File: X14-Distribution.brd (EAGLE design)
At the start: 152.4 x 76.2 mm, 57 parts, among them Q1 310mA/60V/1.6Ω, Q2 IRF1018EPBF, Q3 IRF1018EPBF, Q4 IRF1018EPBF, Q5 IRLML5203, Q6 IRLML5203, Q7 IRLML5203, Q8 IRLML5203, U1 DIST_OR_CONTROL_ALTMK06A-M, U2 DIST_OR_CONTROL_ALTMK06A-M

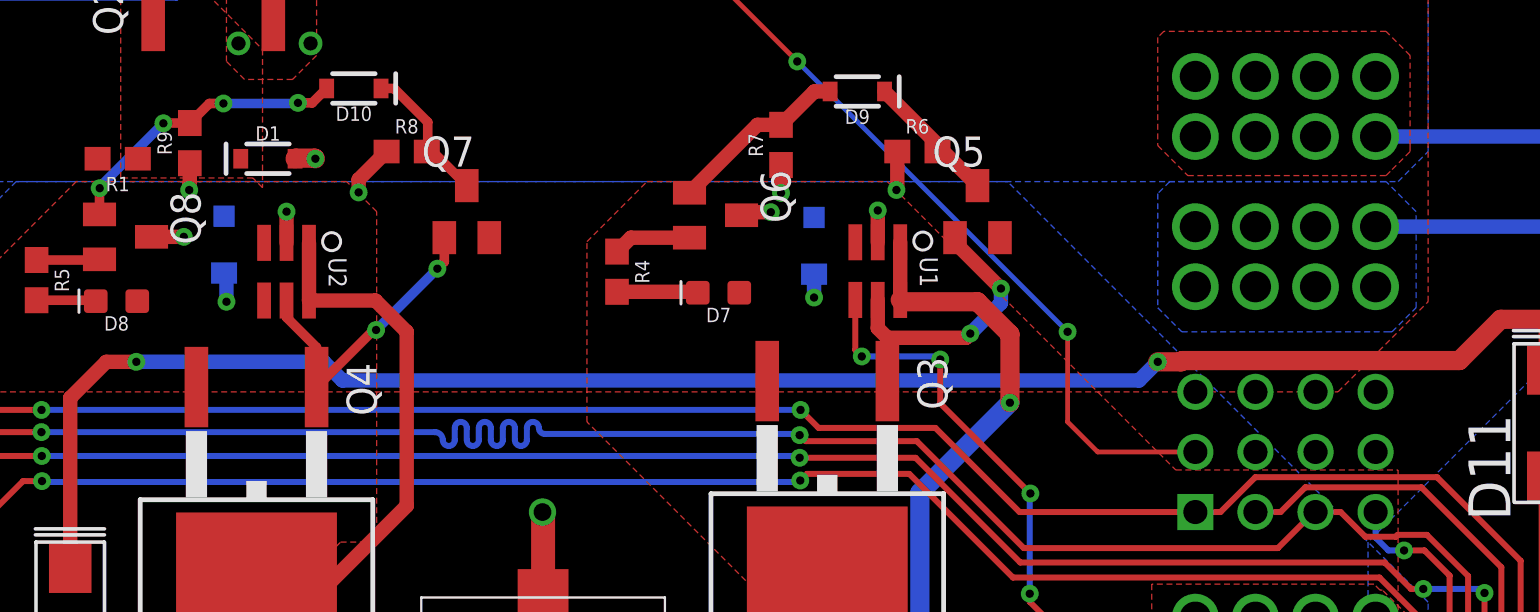
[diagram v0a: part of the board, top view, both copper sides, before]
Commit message: Made changes according to Grant's notes
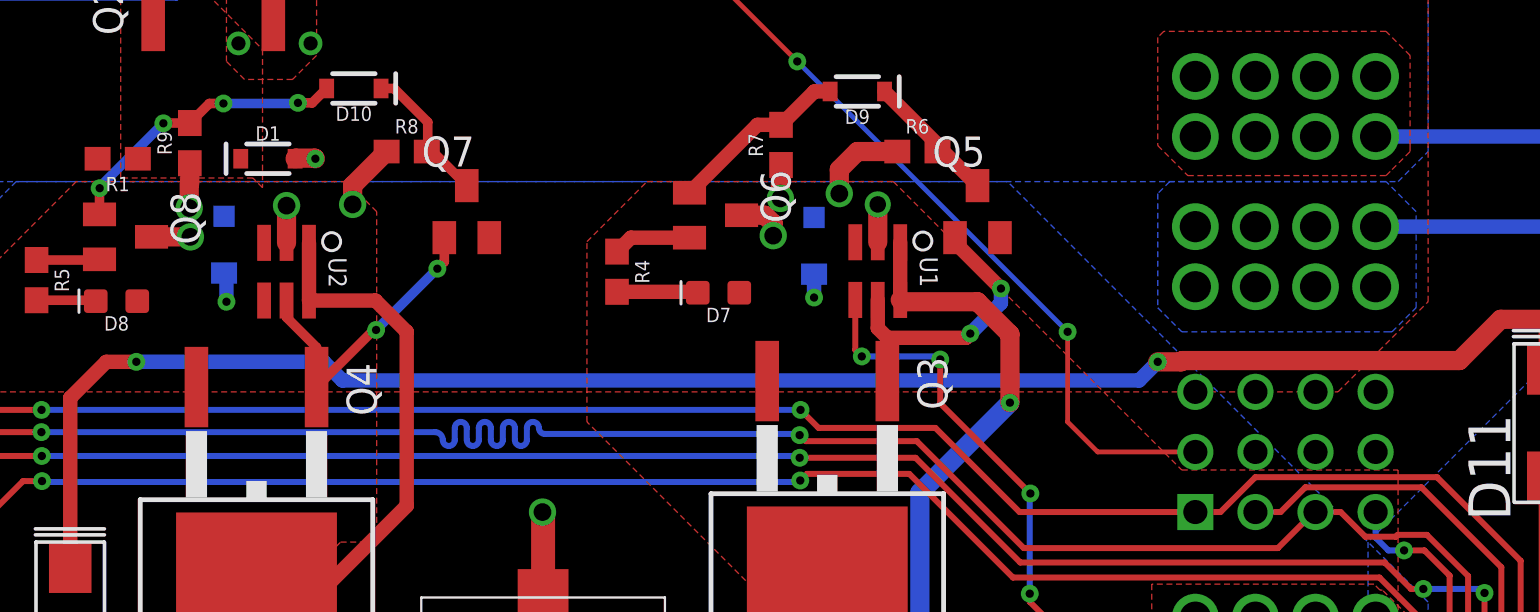
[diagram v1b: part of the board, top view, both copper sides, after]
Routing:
- net 12V_GND: track 63.3 -> 68.5 mm
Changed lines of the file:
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@@
 <wire x1="137.3378" y1="15.0114" x2="138.6586" y2="15.0114" width="0.6096" layer="1"/>
 <wire x1="138.6586" y1="15.0114" x2="140.97" y2="12.7" width="0.6096" layer="1"/>
-<wire x1="65.4128" y1="45.9232" x2="66.7766" y2="45.9232" width="0.6096" layer="1"/>
-<via x="66.7766" y="45.9232" extent="1-16" drill="0.35"/>
-<wire x1="67.0306" y1="49.0356" x2="67.0306" y2="48.1838" width="0.6096" layer="1"/>
+<wire x1="65.4128" y1="45.9232" x2="67.056" y2="45.9232" width="0.8128" layer="1"/>
+<via x="67.056" y="45.9232" extent="1-16" drill="0.75"/>
+<wire x1="67.0306" y1="49.0356" x2="67.0306" y2="48.1838" width="0.8128" layer="1"/>
 <wire x1="67.0306" y1="48.1838" x2="67.0052" y2="48.1584" width="0.6096" layer="1"/>
-<wire x1="67.0052" y1="48.1584" x2="67.0052" y2="47.9044" width="0.6096" layer="1"/>
-<via x="67.0052" y="47.9044" extent="1-16" drill="0.35"/>
-<wire x1="75.35" y1="49.53" x2="74.168" y2="48.348" width="0.6096" layer="1"/>
-<wire x1="74.168" y1="48.348" x2="74.168" y2="47.8028" width="0.6096" layer="1"/>
-<via x="74.168" y="47.8028" extent="1-16" drill="0.35"/>
-<wire x1="71.12" y1="45.6692" x2="71.12" y2="46.99" width="0.6096" layer="1"/>
-<via x="71.12" y="46.99" extent="1-16" drill="0.35"/>
+<wire x1="67.0052" y1="48.1584" x2="67.0052" y2="47.1424" width="0.8128" layer="1"/>
+<via x="67.0052" y="47.1424" extent="1-16" drill="0.75"/>
+<wire x1="75.35" y1="49.53" x2="73.914" y2="48.094" width="0.8128" layer="1"/>
+<wire x1="73.914" y1="48.094" x2="73.914" y2="47.2948" width="0.8128" layer="1"/>
+<via x="73.914" y="47.2948" extent="1-16" drill="0.75"/>
+<wire x1="71.12" y1="45.6692" x2="71.12" y2="47.244" width="0.8128" layer="1"/>
+<via x="71.12" y="47.244" extent="1-16" drill="0.75"/>
 <wire x1="121.0056" y1="13.589" x2="132.8674" y2="13.589" width="0.6096" layer="16"/>
 <wire x1="120.9548" y1="13.6398" x2="121.0056" y2="13.589" width="0.6096" layer="16"/>
 <via x="120.9548" y="13.6398" extent="1-16" drill="0.35"/>
-<wire x1="92.0242" y1="48.9594" x2="92.0242" y2="47.7774" width="0.6096" layer="1"/>
-<via x="92.0242" y="47.7774" extent="1-16" drill="0.35"/>
-<wire x1="90.3556" y1="46.8376" x2="90.4826" y2="46.9646" width="0.6096" layer="1"/>
-<wire x1="90.4826" y1="46.9646" x2="91.5924" y2="46.9646" width="0.6096" layer="1"/>
-<via x="91.5924" y="46.9646" extent="1-16" drill="0.35"/>
-<wire x1="96.94" y1="49.53" x2="96.94" y2="47.9434" width="0.6096" layer="1"/>
-<wire x1="96.94" y1="47.9434" x2="96.901" y2="47.9044" width="0.6096" layer="1"/>
-<via x="96.901" y="47.9044" extent="1-16" drill="0.35"/>
-<wire x1="96.1136" y1="45.6946" x2="96.1136" y2="47.0408" width="0.6096" layer="1"/>
-<via x="96.1136" y="47.0408" extent="1-16" drill="0.35"/>
+<wire x1="92.0242" y1="48.9594" x2="91.9988" y2="48.934" width="0.8128" layer="1"/>
+<wire x1="91.9988" y1="48.934" x2="91.9988" y2="47.5488" width="0.8128" layer="1"/>
+<via x="91.9988" y="47.5488" extent="1-16" drill="0.75"/>
+<wire x1="96.1136" y1="45.6946" x2="96.1136" y2="47.2948" width="0.8128" layer="1"/>
+<via x="96.1136" y="47.2948" extent="1-16" drill="0.7"/>
 <wire x1="114.0206" y1="6.6294" x2="110.5154" y2="6.6294" width="0.6096" layer="1"/>
 <wire x1="110.5154" y1="6.6294" x2="110.49" y2="6.604" width="0.6096" layer="1"/>
@@
 <wire x1="81.9658" y1="34.2646" x2="81.9404" y2="34.29" width="1.016" layer="1"/>
 <via x="81.9404" y="34.29" extent="1-16" drill="0.75"/>
+<wire x1="90.3556" y1="46.8376" x2="91.3384" y2="46.8376" width="0.8128" layer="1"/>
+<wire x1="91.3384" y1="46.8376" x2="91.694" y2="46.482" width="0.8128" layer="1"/>
+<wire x1="91.694" y1="46.482" x2="91.694" y2="45.974" width="0.8128" layer="1"/>
+<via x="91.694" y="45.974" extent="1-16" drill="0.75"/>
+<wire x1="96.94" y1="49.53" x2="95.25" y2="49.53" width="0.8128" layer="1"/>
+<wire x1="95.25" y1="49.53" x2="94.488" y2="48.768" width="0.8128" layer="1"/>
+<wire x1="94.488" y1="48.768" x2="94.488" y2="47.752" width="0.8128" layer="1"/>
+<via x="94.488" y="47.752" extent="1-16" drill="0.75"/>
 </signal>
 <signal name="N$5">
@@
 <vertex x="83.82" y="45.72"/>
 <vertex x="86.36" y="48.26"/>
-<vertex x="96.52" y="48.26"/>
-<vertex x="108.712" y="36.068"/>
+<vertex x="96.774" y="48.26"/>
+<vertex x="108.966" y="36.068"/>
 <vertex x="118.11" y="36.068"/>
 <vertex x="118.11" y="19.05"/>

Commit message: Changed curves back to zigzagy thingys
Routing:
- net CLK: track 127.6 -> 129.5 mm

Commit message: All changes except for bricks outlines
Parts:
- moved R4 0.57 mm to (84.8, 43.9)
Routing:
- net +12V_CONV: track 156.5 -> 160.1 mm
- net N$5: track 5.75 -> 6.94 mm
- net LED_DRIVE_A: track 7.72 -> 8.91 mm
- net 48V_GND: track 77.3 -> 76.1 mm
- net OR_DRIVE_A: track 12.6 -> 13.5 mm
- net +48V: track 71.2 -> 70.2 mm
- net N$3: track 3.31 -> 4.22 mm
- net N$13: track 3.43 -> 4.06 mm
- net N$11: track 6.11 -> 6.72 mm
- net 12V_GND: track 68.5 -> 69.1 mm

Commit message: Made some changes
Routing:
- net +12V_CONV: track 160.1 -> 158.3 mm
- net ON/OFF: track 118.6 -> 118.7 mm, vias 5 -> 7
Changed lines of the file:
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@@
 <vertex x="49.784" y="43.688"/>
 </polygon>
-<wire x1="79.69" y1="45.89" x2="63.1326" y2="49.2252" width="0" layer="19" extent="1-1"/>
 </signal>
 <signal name="N$2">
@@
 <wire x1="45.847" y1="56.007" x2="44.45" y2="54.61" width="0.2032" layer="16"/>
 <via x="92.71" y="53.34" extent="1-16" drill="0.35"/>
-<wire x1="87.3766" y1="58.6734" x2="92.71" y2="53.34" width="0.2032" layer="1"/>
 <wire x1="92.71" y1="53.34" x2="104.14" y2="41.91" width="0.2032" layer="16"/>
 <via x="104.14" y="41.91" extent="1-16" drill="0.35"/>
@@
 <wire x1="66.4718" y1="56.007" x2="67.7926" y2="57.3278" width="0.2032" layer="16"/>
 <via x="67.7926" y="57.3278" extent="1-16" drill="0.35"/>
-<wire x1="87.3766" y1="58.6734" x2="69.1382" y2="58.6734" width="0.2032" layer="1"/>
-<wire x1="67.7926" y1="57.3278" x2="69.1382" y2="58.6734" width="0.2032" layer="1"/>
 <polygon width="0.3048" layer="1" isolate="0.508">
 <vertex x="25.654" y="48.768"/>
@@
 <wire x1="42.418" y1="33.02" x2="46.04" y2="36.642" width="0.254" layer="16"/>
 <wire x1="46.04" y1="36.642" x2="46.04" y2="36.83" width="0.254" layer="16"/>
+<wire x1="69.1388" y1="58.674" x2="73.152" y2="58.674" width="0.2032" layer="1"/>
+<via x="73.152" y="58.674" extent="1-16" drill="0.35"/>
+<wire x1="73.152" y1="58.674" x2="85.09" y2="58.674" width="0.2032" layer="16"/>
+<via x="85.09" y="58.674" extent="1-16" drill="0.35"/>
+<wire x1="85.09" y1="58.674" x2="87.376" y2="58.674" width="0.2032" layer="1"/>
+<wire x1="67.7926" y1="57.3278" x2="69.1388" y2="58.674" width="0.2032" layer="1"/>
+<wire x1="87.376" y1="58.674" x2="92.71" y2="53.34" width="0.2032" layer="1"/>
 </signal>
 <signal name="GND_RAW">
@@
 <wire x1="101.3206" y1="43.1292" x2="101.3206" y2="43.7388" width="0.6096" layer="16"/>
 <via x="101.3206" y="43.7388" extent="1-16" drill="0.35"/>
-<wire x1="99.38" y1="45.6794" x2="99.38" y2="45.89" width="0.6096" layer="1"/>
-<wire x1="96.1136" y1="43.2562" x2="96.1136" y2="42.0624" width="0.6096" layer="1"/>
-<wire x1="96.1136" y1="42.0624" x2="96.266" y2="41.91" width="0.6096" layer="1"/>
-<wire x1="96.52" y1="41.656" x2="96.52" y2="39.826" width="0.6096" layer="1"/>
 <wire x1="100.0252" y1="41.8338" x2="99.949" y2="41.91" width="0.6096" layer="1"/>
 <wire x1="99.949" y1="41.91" x2="96.266" y2="41.91" width="0.6096" layer="1"/>
@@
 <wire x1="99.38" y1="44.5872" x2="99.38" y2="45.89" width="0.6096" layer="1"/>
 <wire x1="99.6442" y1="44.323" x2="99.38" y2="44.5872" width="0.6096" layer="1"/>
-<wire x1="96.1136" y1="43.2562" x2="96.52" y2="41.656" width="0" layer="19" extent="1-1"/>
+<wire x1="96.266" y1="41.91" x2="96.1136" y2="42.0624" width="0.6096" layer="1"/>
+<wire x1="96.1136" y1="42.0624" x2="96.1136" y2="43.2562" width="0.6096" layer="1"/>
+<wire x1="96.52" y1="39.826" x2="96.52" y2="41.656" width="0.6096" layer="1"/>
+<wire x1="96.52" y1="41.656" x2="96.266" y2="41.91" width="0.6096" layer="1"/>
 </signal>
 <signal name="OR_DRIVE_B">
@@
 <contactref element="D8" pad="A"/>
 <contactref element="D14" pad="C"/>
-<polygon width="0.762" layer="1" isolate="0.508" rank="3">
+<polygon width="0.762" layer="1" isolate="0.508" rank="2">
 <vertex x="43.18" y="20.32"/>
 <vertex x="44.45" y="19.05"/>
@@
 <vertex x="73.406" y="33.02"/>
 <vertex x="74.93" y="33.02"/>
-<vertex x="74.93" y="46.99"/>
-<vertex x="73.66" y="48.26"/>
-<vertex x="62.23" y="48.26"/>
-<vertex x="58.42" y="44.45"/>
-<vertex x="58.42" y="39.37"/>
+<vertex x="74.93" y="44.196"/>
+<vertex x="63.246" y="44.196"/>
 <vertex x="55.88" y="36.83"/>
 <vertex x="55.88" y="25.4"/>
@@
 <contactref element="R4" pad="2"/>
 <contactref element="D7" pad="C"/>
-<wire x1="88.5056" y1="43.561" x2="88.4666" y2="43.6" width="0.6096" layer="1"/>
 <wire x1="88.5056" y1="43.561" x2="86.995" y2="43.561" width="0.6096" layer="1"/>
 <wire x1="86.995" y1="43.561" x2="86.36" y2="42.926" width="0.6096" layer="1"/>
@@
 <wire x1="107.95" y1="40.64" x2="109.22" y2="41.91" width="0.8128" layer="1"/>
 <wire x1="121.7676" y1="41.91" x2="124.46" y2="44.6024" width="0.8128" layer="1"/>
-<wire x1="124.46" y1="44.6024" x2="127.9398" y2="48.0822" width="0.8128" layer="1"/>
-<wire x1="127.9398" y1="48.0822" x2="137.5918" y2="57.7342" width="0.8128" layer="1"/>
+<wire x1="124.46" y1="44.6024" x2="126.746" y2="46.8884" width="0.8128" layer="1"/>
 <wire x1="109.22" y1="41.91" x2="121.7676" y2="41.91" width="0.8128" layer="1"/>
 <wire x1="124.46" y1="40.3" x2="124.46" y2="44.6024" width="0.8128" layer="1"/>
-<wire x1="126.746" y1="43.434" x2="128.016" y2="44.704" width="0.8128" layer="1"/>
-<wire x1="128.016" y1="44.704" x2="128.016" y2="48.006" width="0.8128" layer="1"/>
-<wire x1="128.016" y1="48.006" x2="127.9398" y2="48.0822" width="0.8128" layer="1"/>
+<wire x1="126.746" y1="23.7744" x2="126.746" y2="46.8884" width="0.8128" layer="1"/>
 <wire x1="120.6754" y1="17.7038" x2="126.746" y2="23.7744" width="0.8128" layer="1"/>
-<wire x1="126.746" y1="23.7744" x2="126.746" y2="43.434" width="0.8128" layer="1"/>
+<wire x1="126.746" y1="46.8884" x2="137.5918" y2="57.7342" width="0.8128" layer="1"/>
 </signal>
 <signal name="+5V">
